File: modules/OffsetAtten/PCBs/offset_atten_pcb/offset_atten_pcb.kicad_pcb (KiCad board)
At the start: 2 copper layers, 64.8 x 100 mm, 50 parts, among them J1 THONKICONN, J2 THONKICONN, J3 THONKICONN, J4 THONKICONN, J5 Conn_01x08_Pin, J6 Conn_01x08_Socket, J7 Conn_01x07_Pin, J8 Conn_01x07_Socket, J9 Eurorack_2x5_Power, U1 LM324, U2 LM324

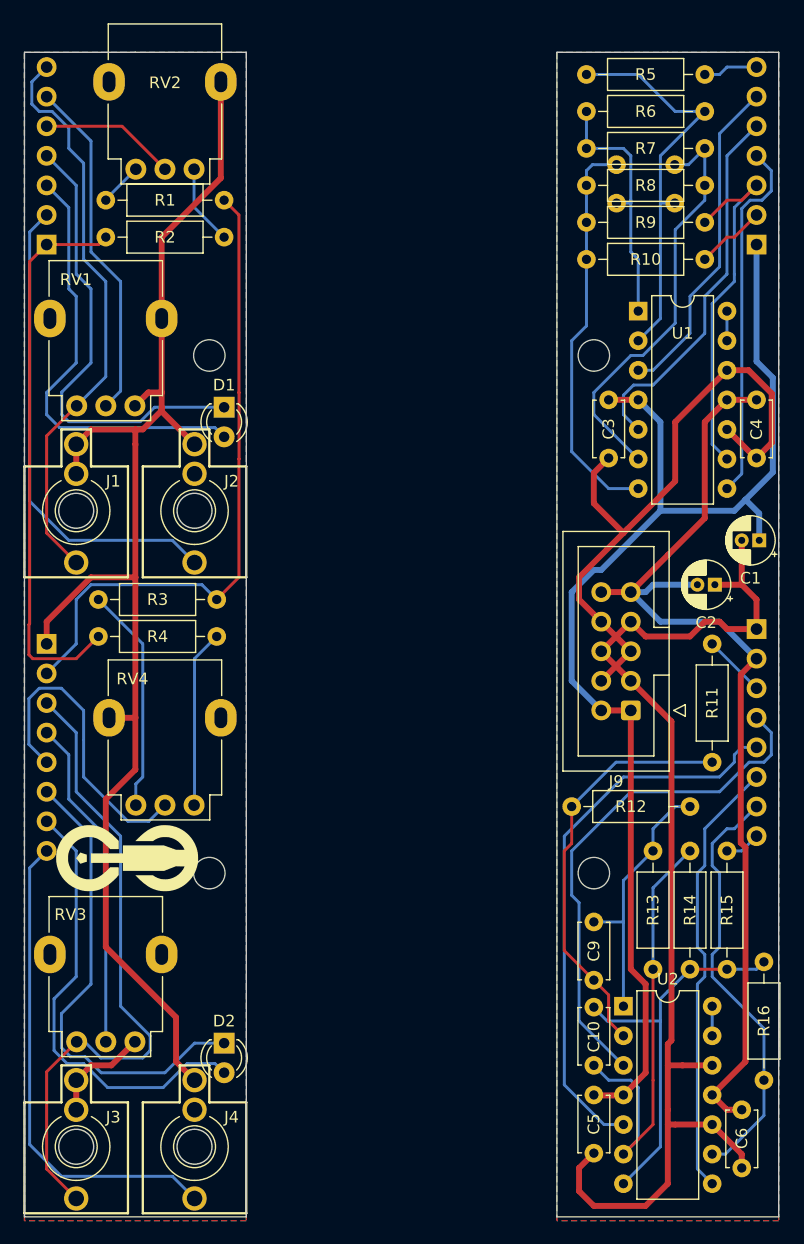
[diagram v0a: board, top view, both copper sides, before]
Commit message: Fix O/A power polarity
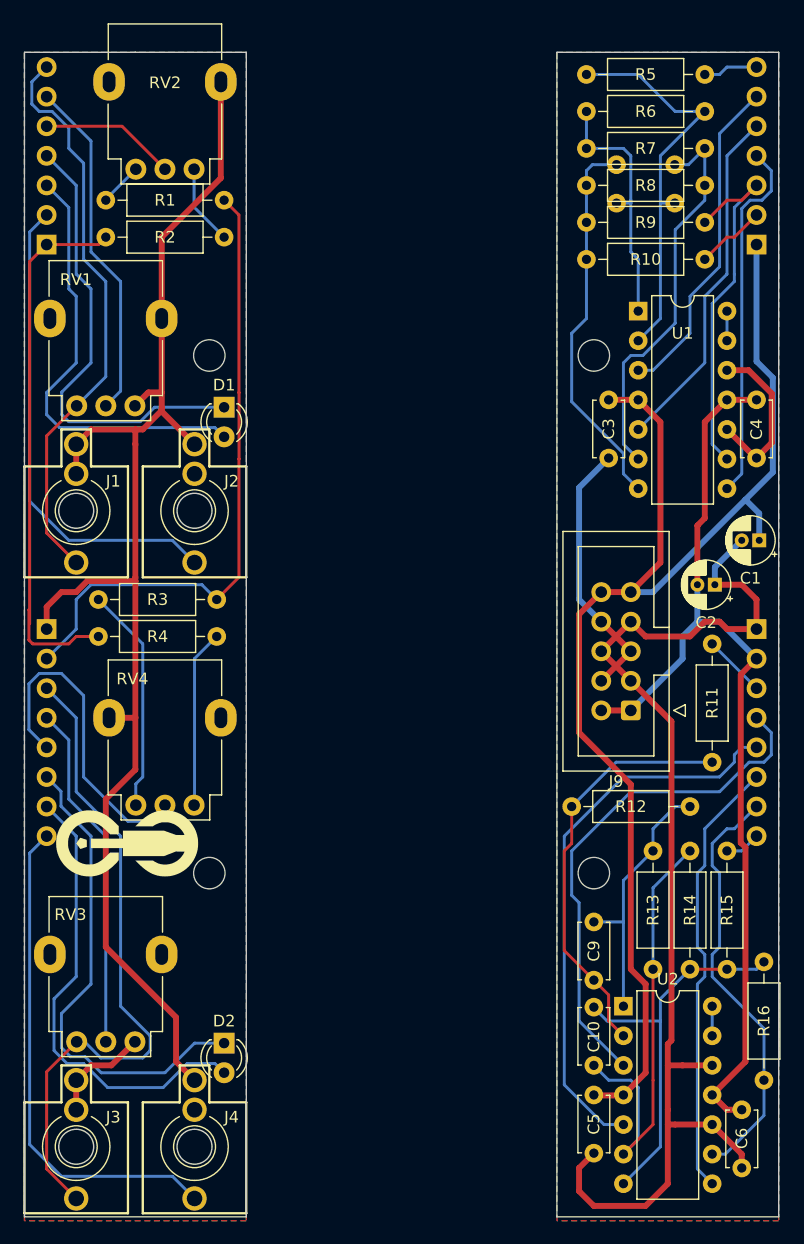
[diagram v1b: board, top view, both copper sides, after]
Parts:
- C7: value 100pF -> 330pF
- moved G1 1.27 mm to (63.3, 131.4)
- moved J6 1.27 mm to (55.9, 113.0)
- renumbered REF** to G1
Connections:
- J9 pad 1: /Main/+12V -> /Main/-12V
- J9 pad 10: /Main/-12V -> /Main/+12V
- J9 pad 2: /Main/+12V -> /Main/-12V
- J9 pad 9: /Main/-12V -> /Main/+12V
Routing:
- net /Main/GND: track 156.8 -> 138.0 mm
- net /Main/+12V: track 109.1 -> 113.6 mm
- net /Main/-12V: track 86.6 -> 84.0 mm
- net Net-(U1B--): track 36.0 -> 33.9 mm
- net /Main/offset_a: track 32.3 -> 30.2 mm
- net Net-(C8-Pad2): track 34.5 -> 33.0 mm
- net /Interface/output_b: track 41.9 -> 43.2 mm
- net /Interface/-12V: track 56.1 -> 54.9 mm
- net /Interface/out_b_led_2: track 40.5 -> 41.8 mm
- net /Interface/atten_input_b: track 28.7 -> 29.9 mm
- net /Interface/offset_b: track 26.8 -> 28.1 mm
- net /Interface/out_b_led_1: track 38.6 -> 39.9 mm
- net /Interface/input_b: track 56.3 -> 57.5 mm
- net /Interface/GND: track 131.8 -> 131.1 mm
- net /Interface/+12V: track 48.1 -> 47.6 mm
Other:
- board text added: "OffsetAtten Back v2.0"
- board text added: "OffsetAtten Front v2.0"
- board text removed: "OffsetAtten Back v0.1"
- board text removed: "OffsetAtten Front v0.1"

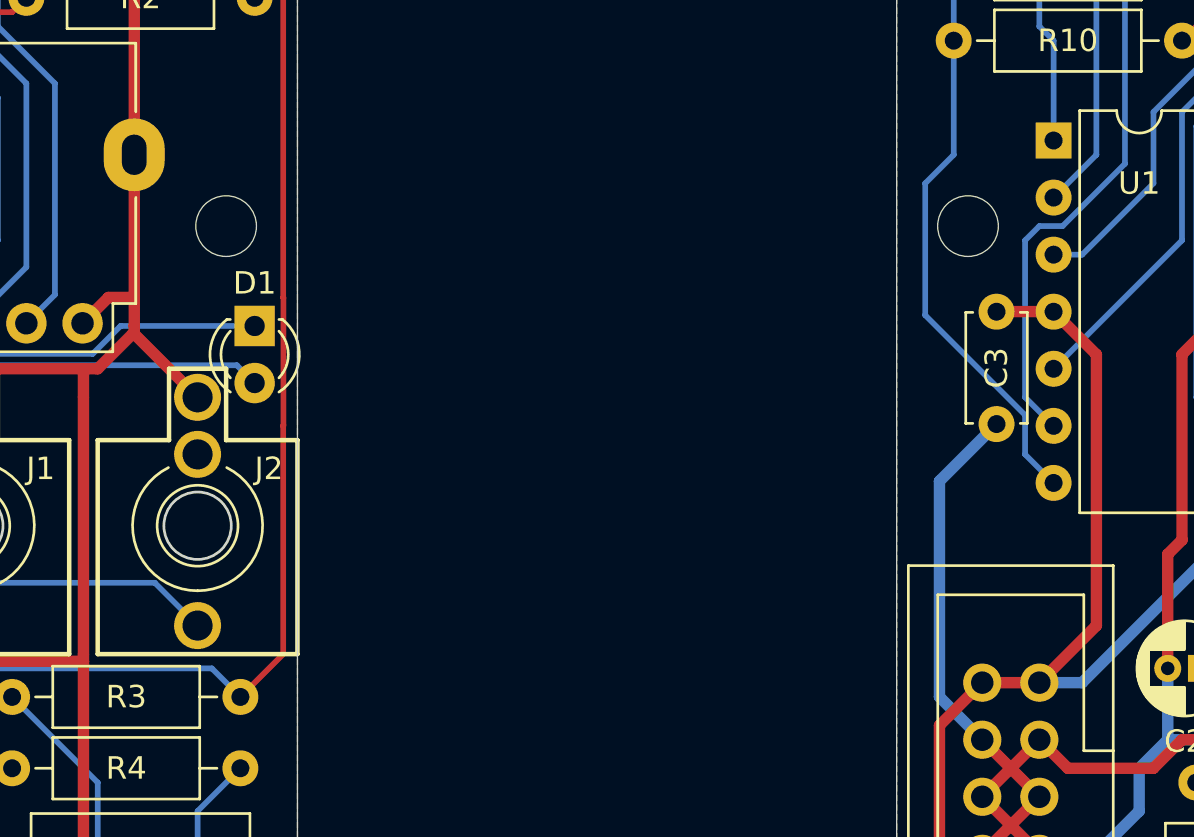
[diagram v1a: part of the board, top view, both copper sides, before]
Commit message: Update standoffs in OA PCB
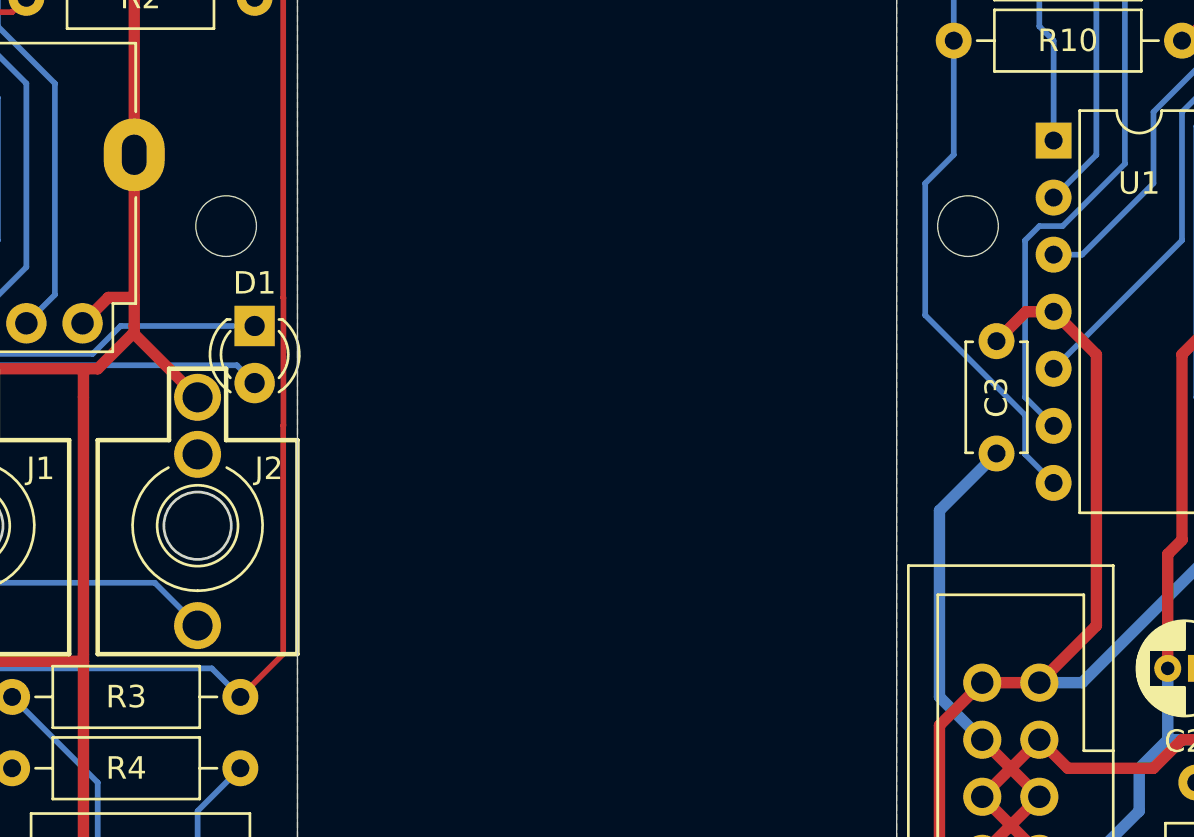
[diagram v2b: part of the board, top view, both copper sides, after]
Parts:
- C10, C7, C8, C9: value 330pF -> 33pF
- H1, H2, H3, H4: value MountingHole -> M3x11mm
- R11, R12, R13, R14, R5, R6, R7, R8, R9: value 10k -> 100k
- moved C3 1.31 mm to (104.1, 94.7)
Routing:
- net /Main/GND: track 138.0 -> 136.7 mm
- net /Interface/GND: track 131.1 -> 130.2 mm
- net /Main/+12V: track 113.6 -> 114.2 mm

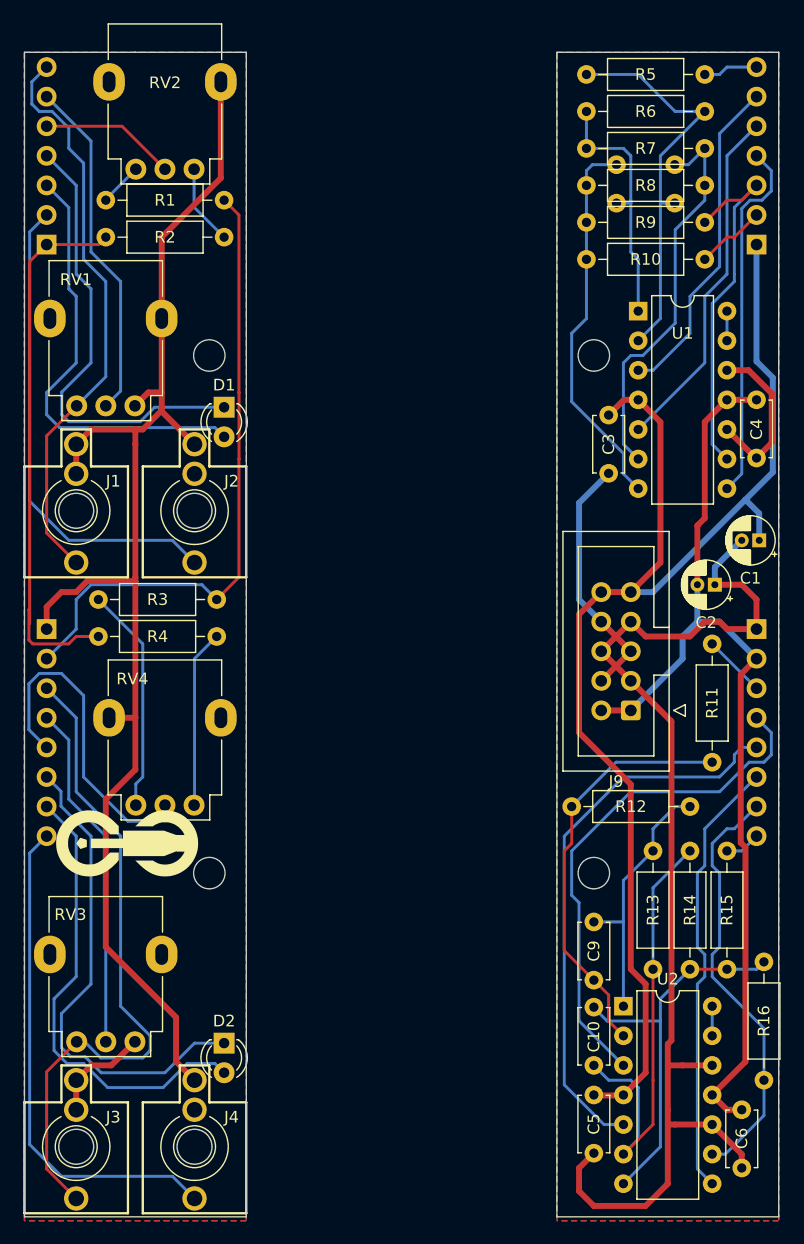
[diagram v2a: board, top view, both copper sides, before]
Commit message: Add buffer to O/A; (see #67) closes #62
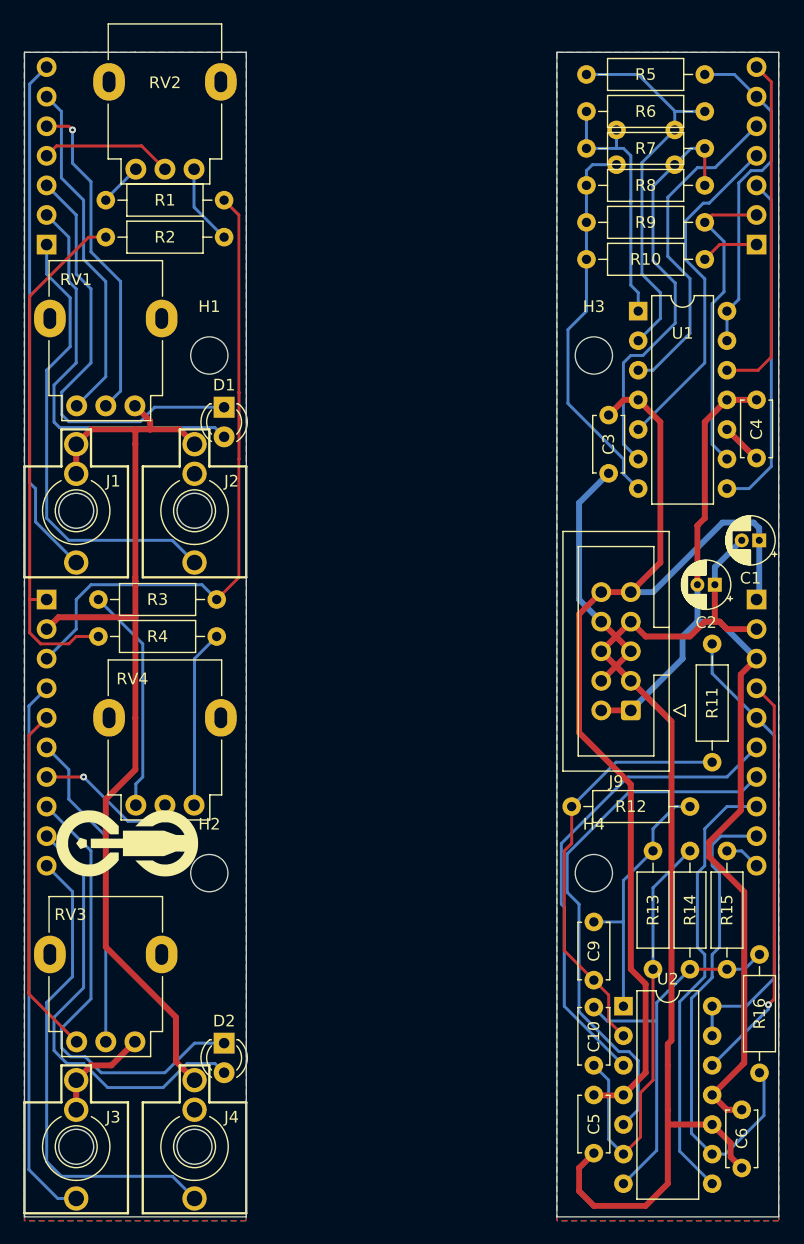
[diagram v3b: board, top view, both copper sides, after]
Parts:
- H1, H2, H3, H4: footprint MountingHole:MountingHole_2.7mm_M2.5 -> MountingHole:MountingHole_3.2mm_M3
- J5: value Conn_01x08_Pin -> Conn_01x10_Pin; footprint Connector_PinSocket_2.54mm:PinSocket_1x08_P2.54mm_Vertical -> Connector_PinSocket_2.54mm:PinSocket_1x10_P2.54mm_Vertical
- J6: value Conn_01x08_Socket -> Conn_01x10_Socket; footprint Connector_PinSocket_2.54mm:PinSocket_1x08_P2.54mm_Vertical -> Connector_PinSocket_2.54mm:PinSocket_1x10_P2.54mm_Vertical
- moved C7 6.29 mm to (109.8, 70.2)
- moved J5 2.54 mm to (116.8, 110.5)
- moved J6 2.54 mm to (55.9, 110.5)
- moved R16 0.74 mm to (117.1, 151.1)
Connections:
- J5 pad 1: /Main/GND -> /Main/+12V
- J5 pad 2: /Main/-12V -> /Main/GND
- J5 pad 3: /Main/input_b -> /Main/-12V
- J5 pad 4: /Main/atten_input_b -> /Main/input_b
- J5 pad 5: /Main/offset_b -> /Main/buffered_input_b
- J5 pad 6: /Main/out_b_led_2 -> /Main/atten_input_b
- J5 pad 7: /Main/out_b_led_1 -> /Main/offset_b
- J5 pad 8: /Main/output_b -> /Main/out_b_led_2
- J6 pad 1: /Interface/GND -> /Interface/+12V
- J6 pad 2: /Interface/-12V -> /Interface/GND
- J6 pad 3: /Interface/input_b -> /Interface/-12V
- J6 pad 4: /Interface/atten_input_b -> /Interface/input_b
- J6 pad 5: /Interface/offset_b -> /Interface/buffered_input_b
- J6 pad 6: /Interface/out_b_led_2 -> /Interface/atten_input_b
- J6 pad 7: /Interface/out_b_led_1 -> /Interface/offset_b
- J6 pad 8: /Interface/output_b -> /Interface/out_b_led_2
- J7 pad 1: /Main/+12V -> /Main/output_a
- J7 pad 2: /Main/output_a -> /Main/out_a_led_1
- J7 pad 3: /Main/out_a_led_1 -> /Main/out_a_led_2
- J7 pad 4: /Main/out_a_led_2 -> /Main/offset_a
- J7 pad 5: /Main/offset_a -> /Main/atten_input_a
- J7 pad 6: /Main/atten_input_a -> /Main/buffered_input_a
- J8 pad 1: /Interface/+12V -> /Interface/output_a
- J8 pad 2: /Interface/output_a -> /Interface/out_a_led_1
- J8 pad 3: /Interface/out_a_led_1 -> /Interface/out_a_led_2
- J8 pad 4: /Interface/out_a_led_2 -> /Interface/offset_a
- J8 pad 5: /Interface/offset_a -> /Interface/atten_input_a
- J8 pad 6: /Interface/atten_input_a -> /Interface/buffered_input_a
- R11 pad 2: /Main/input_b -> /Main/buffered_input_b
- R5 pad 1: /Main/input_a -> /Main/buffered_input_a
- RV1 pad 1: /Interface/input_a -> /Interface/buffered_input_a
- RV3 pad 1: /Interface/input_b -> /Interface/buffered_input_b
- RV3 pad MP: /Interface/GND -> (no net)
- U1 pad 12: /Main/GND -> /Main/input_a
- U1 pad 13: Net-(U1D--) -> /Main/buffered_input_a
- U1 pad 14: Net-(U1D--) -> /Main/buffered_input_a
- U2 pad 12: /Main/GND -> /Main/input_b
- U2 pad 13: Net-(U2D--) -> /Main/buffered_input_b
- U2 pad 14: Net-(U2D--) -> /Main/buffered_input_b
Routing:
- net /Main/buffered_input_b: track 0.00 -> 39.8 mm
- net /Interface/GND: track 130.2 -> 93.4 mm
- net /Interface/buffered_input_b: track 0.00 -> 30.8 mm
- net /Main/input_b: track 5.39 -> 35.2 mm, vias 0 -> 1
- net /Interface/buffered_input_a: track 0.00 -> 29.7 mm
- net /Main/buffered_input_a: track 0.00 -> 28.8 mm
- net /Main/input_a: track 4.71 -> 29.7 mm
- net /Main/+12V: track 114.2 -> 93.2 mm
- net /Main/GND: track 136.7 -> 118.6 mm
- net /Interface/offset_b: track 28.1 -> 12.3 mm, vias 0 -> 1
- net /Interface/input_b: track 57.5 -> 47.1 mm
- net /Main/out_b_led_1: track 36.7 -> 41.5 mm
- net /Interface/input_a: track 49.6 -> 44.8 mm
- net /Main/out_a_led_1: track 31.4 -> 26.7 mm
- net /Main/atten_input_b: track 44.5 -> 41.4 mm
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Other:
- board text added: "OffsetAtten Back v2.1"
- board text added: "OffsetAtten Front v2.1"
- board text removed: "OffsetAtten Back v2.0"
- board text removed: "OffsetAtten Front v2.0"
